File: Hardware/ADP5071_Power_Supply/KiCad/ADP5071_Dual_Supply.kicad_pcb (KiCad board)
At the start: 2 copper layers, 59.4 x 36.9 mm, 43 parts, among them J1 MountingPin, J2 Screw_Terminal_01x02, J3 Conn_01x03_Pin, J4 MountingPin, J5 MountingPin, J6 MountingPin, U1 ADP5071AREZ

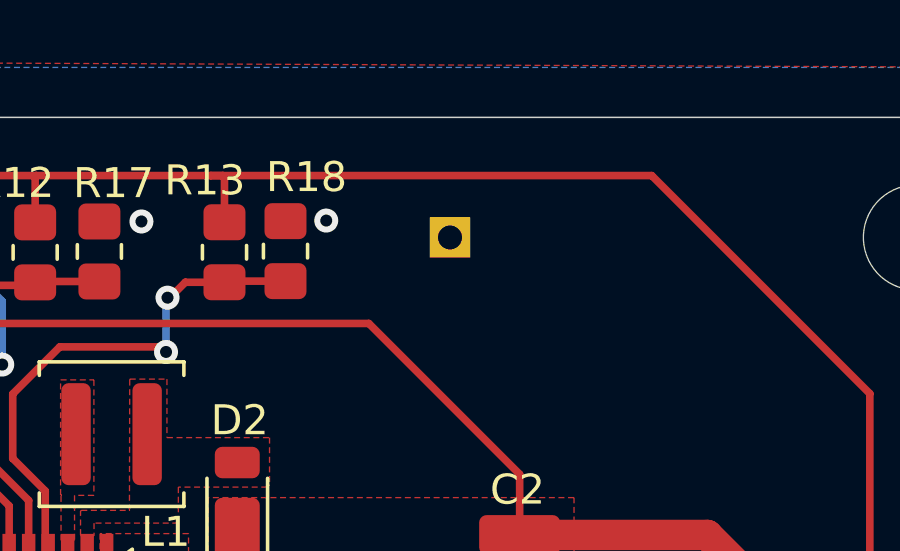
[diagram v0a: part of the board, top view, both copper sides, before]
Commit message: Fixed mounting asymmetry
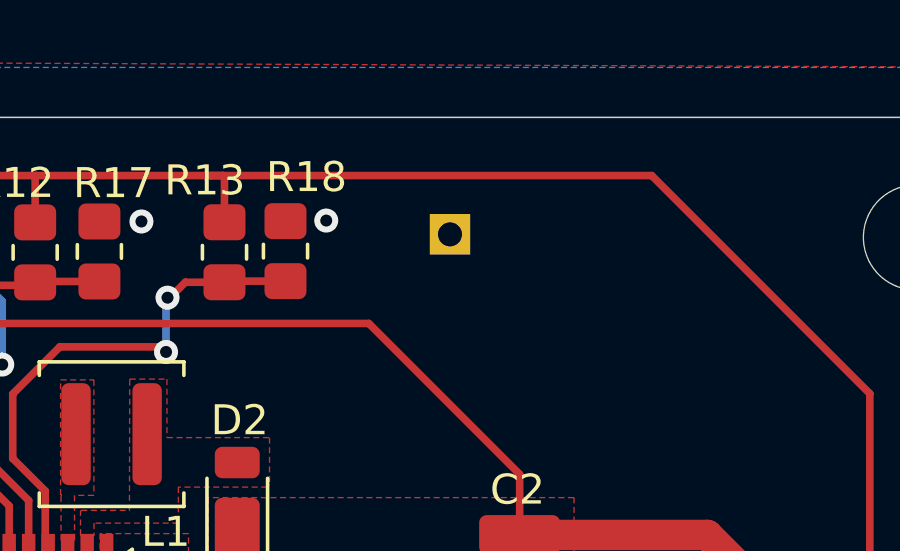
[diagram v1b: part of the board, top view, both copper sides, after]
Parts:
- moved J5 0.10 mm to (93.0, 69.0)
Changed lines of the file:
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@@
 	(footprint "Connector_PinSocket_2.00mm:PinSocket_1x01_P2.00mm_Vertical"
 		(layer "B.Cu")
-		(at 93 69.1034)
+		(at 93 69.0004)
 		(descr "Through hole straight socket strip, 1x01, 2.00mm pitch, single row (from Kicad 4.0.7), script generated")
 		(tags "Through hole socket strip THT 1x01 2.00mm single row")

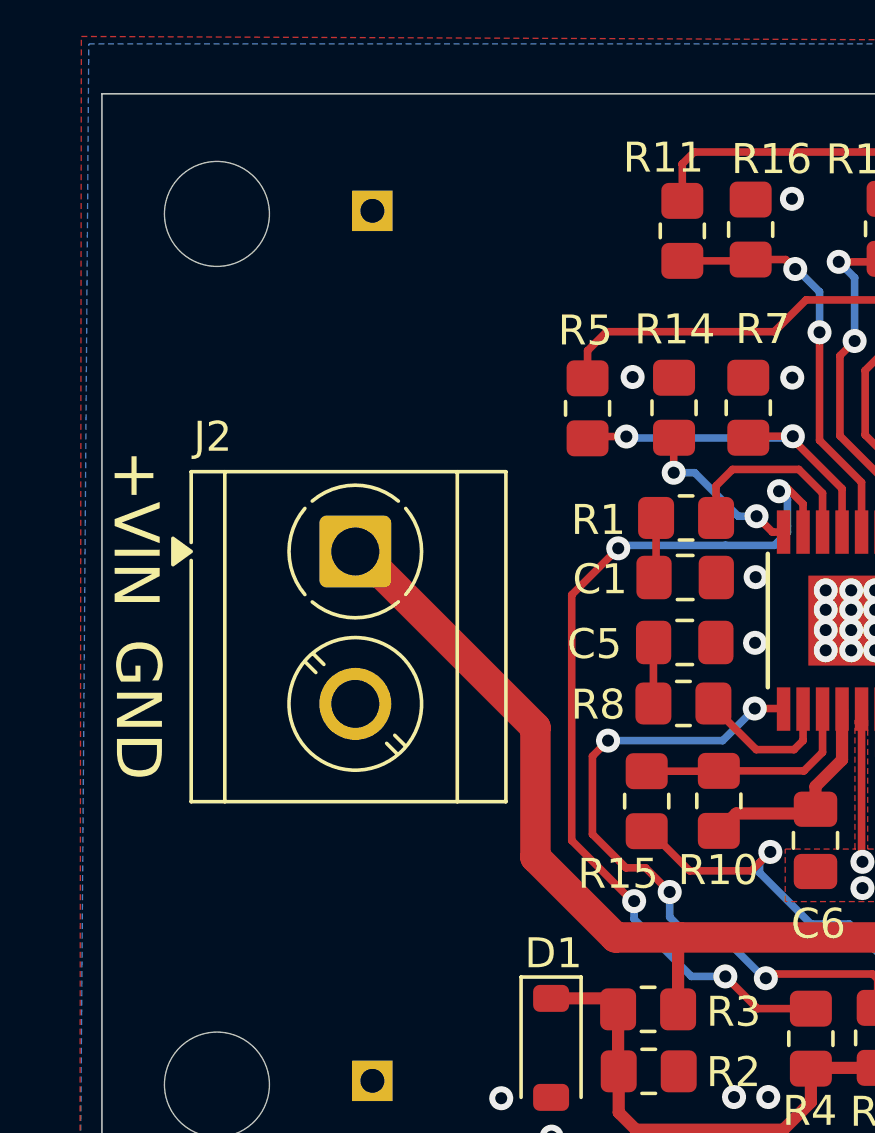
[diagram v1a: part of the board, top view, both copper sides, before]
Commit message: Waveguide + ground planes and P.S. daughter board modification
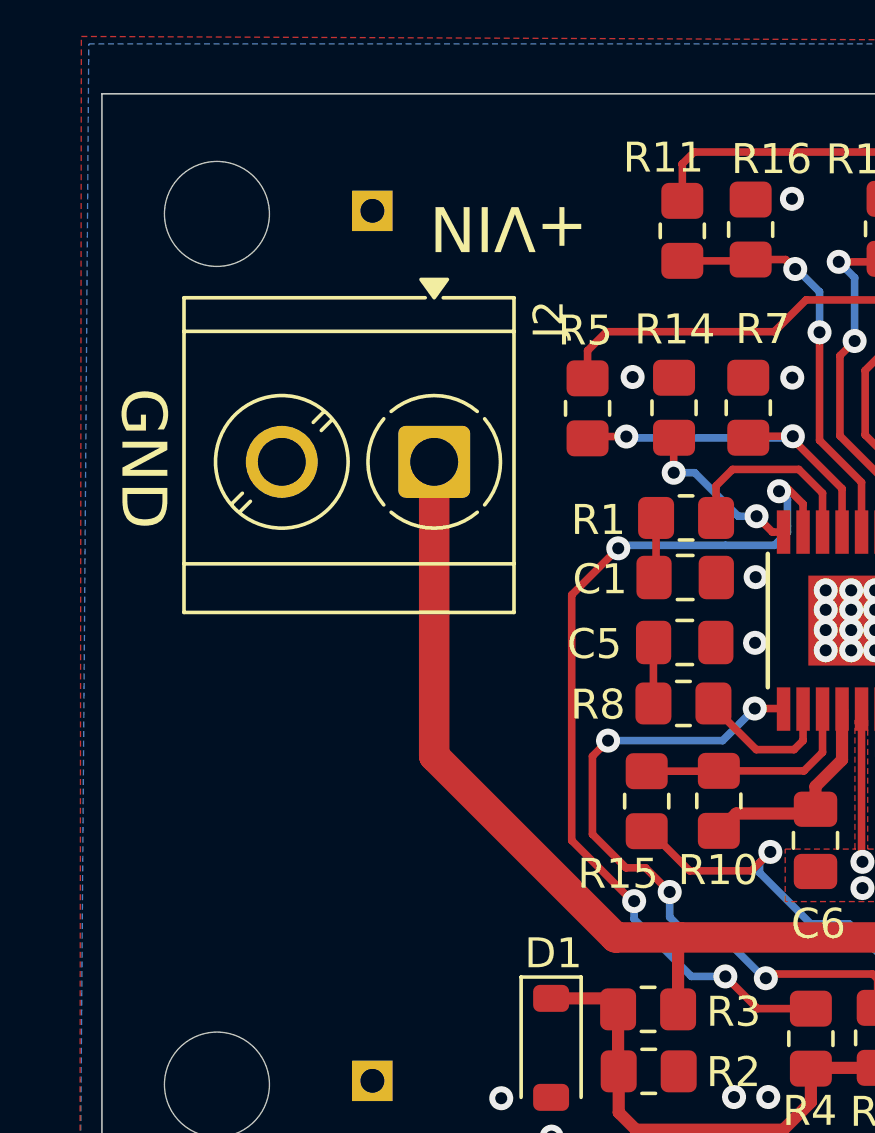
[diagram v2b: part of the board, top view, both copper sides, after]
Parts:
- moved J2 3.98 mm to (64.1, 77.4), turned to 180 degrees
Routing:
- net /VIN: track 49.9 -> 51.7 mm
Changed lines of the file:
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@@
 	(footprint "TerminalBlock_CUI:TerminalBlock_CUI_TB007-508-02_1x02_P5.08mm_Horizontal"
 		(layer "F.Cu")
-		(at 61.4296 80.3554 -90)
+		(at 64.060001 77.3675 180)
 		(descr "Terminal Block CUI TB007-508-02, 2 pins, pitch 5.08mm, size 10.8x10.2mm, drill diameter 1.6mm, pad diameter 2.4mm, https://www.cuidevices.com/product/resource/tb007-508.pdf, script-generated using https://gitlab.com/kicad/libraries/kicad-footprint-generator/scripts/TerminalBlock_CUI")
 		(tags "THT Terminal Block CUI TB007-508-02 pitch 5.08mm size 10.8x10.2mm drill 1.6mm pad 2.4mm")
 		(property "Reference" "J2"
-			(at -3.8206 4.7498 180)
+			(at -3.8206 4.7498 90)
 			(layer "F.SilkS")
 			(effects
@@
 		)
 		(property "Value" "Screw_Terminal_01x02"
-			(at 2.84 6.47 90)
+			(at 2.84 6.47 0)
 			(layer "F.Fab")
 			(effects
@@
 		)
 		(property "Datasheet" "~"
-			(at 0 0 90)
+			(at 0 0 0)
 			(layer "F.Fab")
 			(hide yes)
@@
 		)
 		(property "Description" "Generic screw terminal, single row, 01x02, script generated (kicad-library-utils/schlib/autogen/connector/)"
-			(at 0 0 90)
+			(at 0 0 0)
 			(layer "F.Fab")
 			(hide yes)
@@
 		(attr through_hole)
 		(fp_line
-			(start -2.66 5.47)
-			(end -0.3 5.47)
+			(start 8.340001 -5.02)
+			(end 8.34 5.470001)
 			(stroke
 				(width 0.12)
@@
 		)
 		(fp_line
-			(start 0.3 5.47)
-			(end 8.34 5.470001)
+			(start 6.756 -1.406001)
+			(end 6.394999 -1.045)
 			(stroke
 				(width 0.12)
@@
 		)
 		(fp_line
-			(start -2.660001 4.35)
-			(end 8.34 4.35)
+			(start 6.486001 -1.676)
+			(end 6.126001 -1.315)
 			(stroke
 				(width 0.12)
@@
 		)
 		(fp_line
-			(start 6.756 -1.406001)
-			(end 6.394999 -1.045)
+			(start 0.3 5.47)
+			(end 8.34 5.470001)
 			(stroke
 				(width 0.12)
@@
 		)
 		(fp_line
-			(start 6.486001 -1.676)
-			(end 6.126001 -1.315)
+			(start -2.66 5.47)
+			(end -0.3 5.47)
 			(stroke
 				(width 0.12)
@@
 		(fp_line
 			(start -2.66 -5.02)
-			(end -2.66 5.47)
+			(end 8.340001 -5.02)
 			(stroke
 				(width 0.12)
@@
 		(fp_line
 			(start -2.66 -5.02)
-			(end 8.340001 -5.02)
+			(end -2.66 5.47)
 			(stroke
 				(width 0.12)
@@
 		)
 		(fp_line
-			(start 8.340001 -5.02)
-			(end 8.34 5.470001)
+			(start -2.660001 4.35)
+			(end 8.34 4.35)
 			(stroke
 				(width 0.12)
@@
 		)
 		(fp_arc
-			(start 1.436 1.68)
-			(mid 0.000105 2.21009)
-			(end -1.43584 1.680136)
+			(start 1.68 -1.436)
+			(mid 2.21009 -0.000105)
+			(end 1.680136 1.43584)
 			(stroke
 				(width 0.12)
@@
 		)
 		(fp_arc
-			(start -1.68 1.436)
-			(mid -2.21009 0.000105)
-			(end -1.680136 -1.43584)
+			(start 1.436 1.68)
+			(mid 0.000105 2.21009)
+			(end -1.43584 1.680136)
 			(stroke
 				(width 0.12)
@@
 		)
 		(fp_arc
-			(start 1.68 -1.436)
-			(mid 2.21009 -0.000105)
-			(end 1.680136 1.43584)
+			(start -1.436 -1.68)
+			(mid -0.000105 -2.21009)
+			(end 1.43584 -1.680136)
 			(stroke
 				(width 0.12)
@@
 		)
 		(fp_arc
-			(start -1.436 -1.68)
-			(mid -0.000105 -2.21009)
-			(end 1.43584 -1.680136)
+			(start -1.68 1.436)
+			(mid -2.21009 0.000105)
+			(end -1.680136 -1.43584)
 			(stroke
 				(width 0.12)
@@
 		)
 		(fp_line
-			(start -3.04 5.85)
-			(end 8.72 5.85)
+			(start 8.720001 -5.4)
+			(end -3.04 -5.4)
 			(stroke
 				(width 0.05)
@@
 		)
 		(fp_line
-			(start -3.04 -5.4)
-			(end -3.04 5.85)
+			(start -3.04 5.85)
+			(end 8.72 5.85)
 			(stroke
 				(width 0.05)
@@
 		)
 		(fp_line
-			(start 8.720001 -5.4)
-			(end -3.04 -5.4)
+			(start -3.04 -5.4)
+			(end -3.04 5.85)
 			(stroke
 				(width 0.05)
@@
 		)
 		(fp_line
-			(start -1.54 5.35)
-			(end -2.54 4.35)
+			(start 8.22 5.35)
+			(end -1.54 5.35)
 			(stroke
 				(width 0.1)
@@
 		)
 		(fp_line
-			(start 8.22 5.35)
-			(end -1.54 5.35)
+			(start 8.22 -4.9)
+			(end 8.22 5.35)
 			(stroke
 				(width 0.1)
@@
 		)
 		(fp_line
-			(start -2.54 4.35)
-			(end 8.22 4.35)
+			(start 6.483 -1.177)
+			(end 3.903 1.403)
 			(stroke
 				(width 0.1)
@@
 		)
 		(fp_line
-			(start -2.54 4.35)
-			(end -2.54 -4.9)
+			(start 6.257 -1.403)
+			(end 3.677 1.177)
 			(stroke
 				(width 0.1)
@@
 		)
 		(fp_line
-			(start 6.483 -1.177)
-			(end 3.903 1.403)
+			(start 1.177 -1.403)
+			(end -1.403 1.177)
 			(stroke
 				(width 0.1)
@@
 		)
 		(fp_line
-			(start 1.177 -1.403)
-			(end -1.403 1.177)
+			(start -1.54 5.35)
+			(end -2.54 4.35)
 			(stroke
 				(width 0.1)
@@
 		)
 		(fp_line
-			(start 6.257 -1.403)
-			(end 3.677 1.177)
+			(start -2.54 4.35)
+			(end 8.22 4.35)
 			(stroke
 				(width 0.1)
@@
 		)
 		(fp_line
-			(start -2.54 -3.4)
-			(end 8.22 -3.4)
+			(start -2.54 4.35)
+			(end -2.54 -4.9)
 			(stroke
 				(width 0.1)
@@
 		)
 		(fp_line
-			(start -2.54 -4.9)
-			(end 8.22 -4.9)
+			(start -2.54 -3.4)
+			(end 8.22 -3.4)
 			(stroke
 				(width 0.1)
@@
 		)
 		(fp_line
-			(start 8.22 -4.9)
-			(end 8.22 5.35)
+			(start -2.54 -4.9)
+			(end 8.22 -4.9)
 			(stroke
 				(width 0.1)
@@
 		)
 		(fp_circle
-			(center 0 0)
-			(end 1.850001 0)
+			(center 5.079999 0)
+			(end 6.93 0)
 			(stroke
 				(width 0.1)
@@
 		)
 		(fp_circle
-			(center 5.079999 0)
-			(end 6.93 0)
+			(center 0 0)
+			(end 1.850001 0)
 			(stroke
 				(width 0.1)
@@
 		)
 		(fp_text user "${REFERENCE}"
-			(at 2.84 0.225 90)
+			(at 2.84 0.225 0)
 			(layer "F.Fab")
 			(effects
@@
 		)
 		(pad "1" thru_hole roundrect
-			(at 0 0 270)
+			(at 0 0 180)
 			(size 2.4 2.4)
 			(drill 1.6)
@@
 		)
 		(pad "2" thru_hole circle
-			(at 5.079999 0 270)
+			(at 5.079999 0 180)
 			(size 2.4 2.4)
 			(drill 1.6)
@@
 	)
 	(gr_text "+VIN"
-		(at 54.103 79.602 270)
+		(at 66.54 69.57 180)
 		(layer "F.SilkS")
 		(effects
@@
 	)
 	(gr_text "GND"
-		(at 54.178 85.627 270)
+		(at 54.36 77.26 270)
 		(layer "F.SilkS")
 		(effects
@@
 	)
 	(segment
+		(start 64.060001 87.175601)
+		(end 64.060001 77.3675)
+		(width 1.016)
+		(layer "F.Cu")
+		(net 4)
+	)
+	(segment
 		(start 80.3944 94.1)
 		(end 80.3944 93.22)
@@
 	)
 	(segment
-		(start 67.4344 90.55)
-		(end 70.1044 93.22)
-		(width 1.016)
-		(layer "F.Cu")
-		(net 4)
-	)
-	(segment
 		(start 80.148897 87.355503)
 		(end 80.442094 87.6487)
@@
 	)
 	(segment
-		(start 67.4344 86.22)
-		(end 67.4344 90.55)
-		(width 1.016)
-		(layer "F.Cu")
-		(net 4)
-	)
-	(segment
 		(start 79.605 85.6084)
 		(end 79.605 86.811606)
@@
 	)
 	(segment
+		(start 72.2444 93.22)
+		(end 70.1044 93.22)
+		(width 1.016)
+		(layer "F.Cu")
+		(net 4)
+	)
+	(segment
 		(start 80.905 87.5393)
 		(end 81.0144 87.6487)
@@
 	)
 	(segment
+		(start 70.1044 93.22)
+		(end 64.060001 87.175601)
+		(width 1.016)
+		(layer "F.Cu")
+		(net 4)
+	)
+	(segment
 		(start 80.905 85.6084)
 		(end 80.905 87.5393)
@@
 	)
 	(segment
-		(start 61.5698 80.3554)
-		(end 67.4344 86.22)
-		(width 1.016)
-		(layer "F.Cu")
-		(net 4)
-	)
-	(segment
 		(start 80.3944 93.22)
 		(end 80.8444 93.22)
@@
 	)
 	(segment
-		(start 70.1044 93.22)
-		(end 72.2444 93.22)
-		(width 1.016)
-		(layer "F.Cu")
-		(net 4)
-	)
-	(segment
 		(start 80.671602 94.377202)
 		(end 80.3944 94.1)
@@
 		(layer "F.Cu")
 		(net 4)
-	)
-	(segment
-		(start 61.4296 80.3554)
-		(end 61.5698 80.3554)
-		(width 1.016)
-		(layer "F.Cu")
-		(net 4)

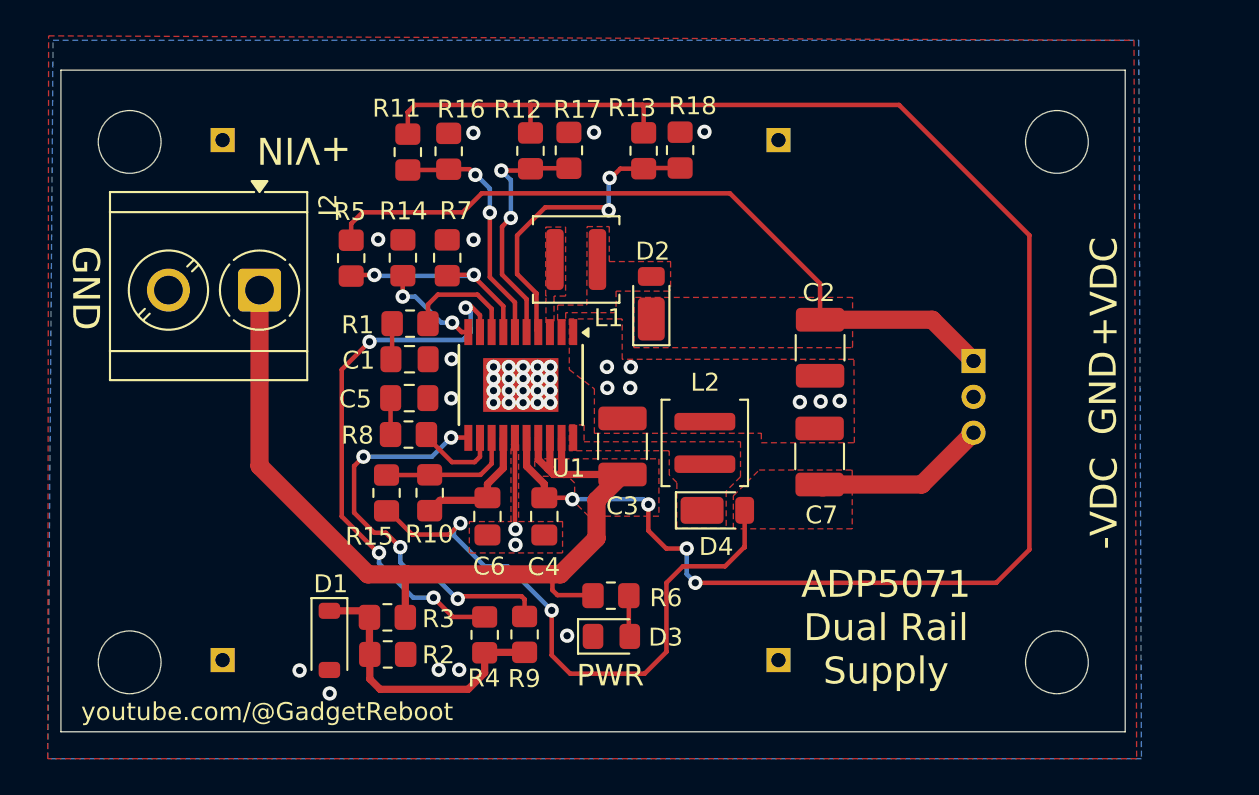
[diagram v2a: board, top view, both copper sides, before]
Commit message: Ease of construction, added new layers, prelimininary routing.
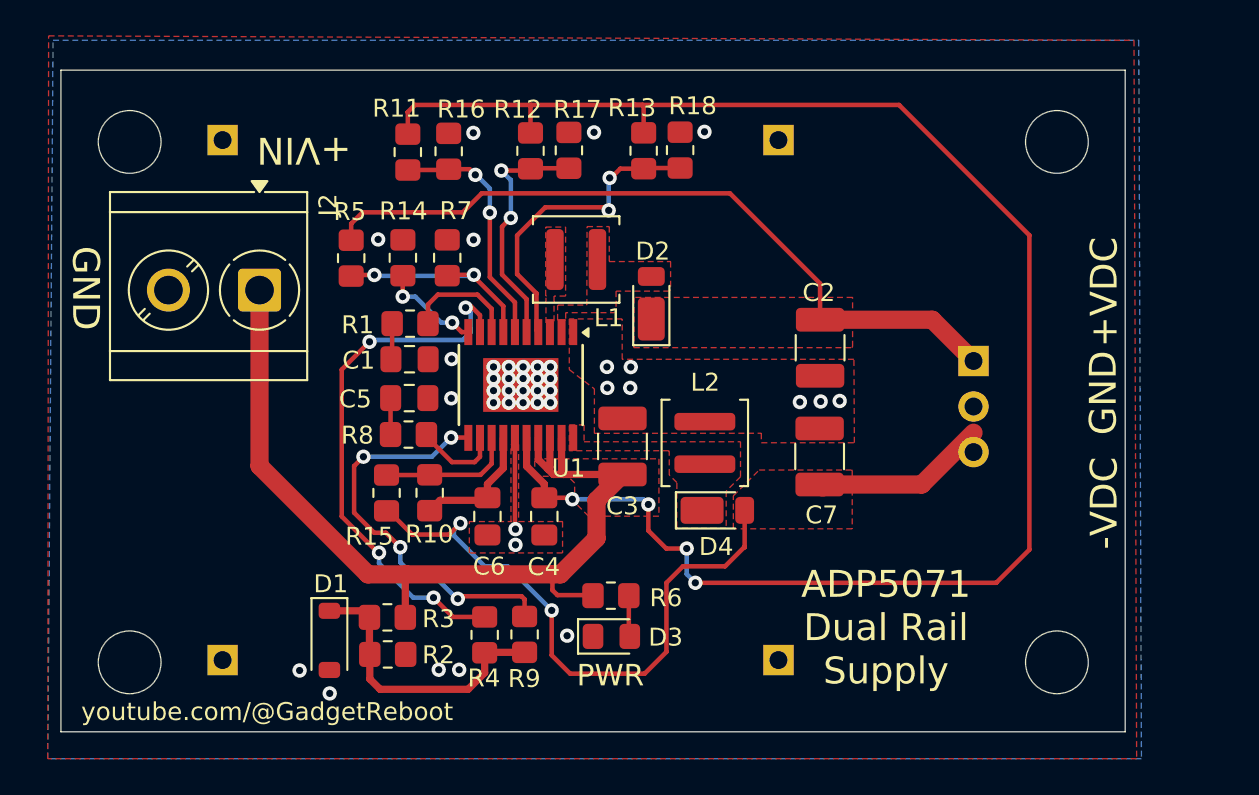
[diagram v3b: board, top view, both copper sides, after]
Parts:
- J1, J4, J5, J6: footprint Connector_PinSocket_2.00mm:PinSocket_1x01_P2.00mm_Vertical -> Connector_PinSocket_2.54mm:PinSocket_1x01_P2.54mm_Vertical
- J3: footprint Connector_PinHeader_2.00mm:PinHeader_1x03_P2.00mm_Vertical -> Connector_PinHeader_2.54mm:PinHeader_1x03_P2.54mm_Vertical

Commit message: added connector for dual board power delivery
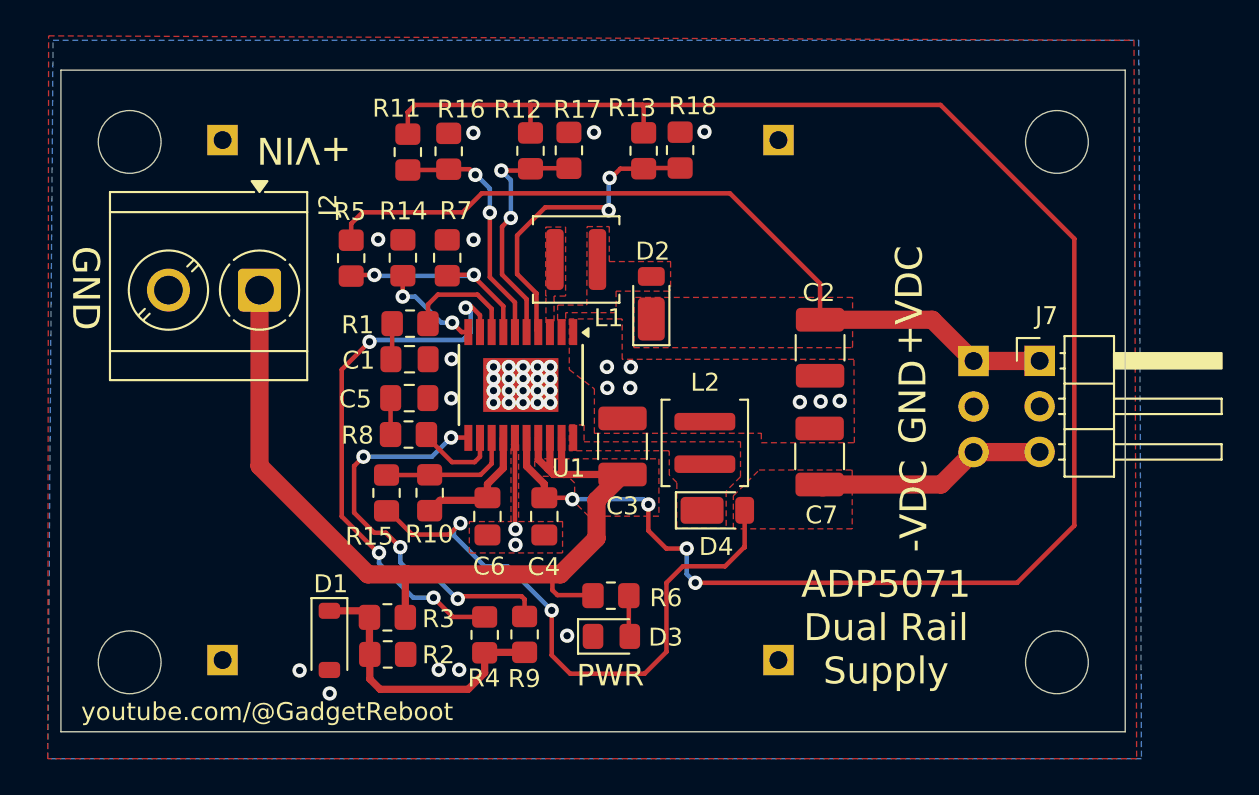
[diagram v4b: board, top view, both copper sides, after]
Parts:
- added J7: Conn_01x03_Pin, Connector_PinHeader_2.54mm:PinHeader_1x03_P2.54mm_Horizontal, F.Cu at (107.6, 81.3)
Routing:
- net Net-(U1-VREG): track 95.4 -> 99.5 mm
- net +VDC: track 41.4 -> 45.1 mm, vias 0 -> 21
- net -VDC: track 43.9 -> 47.2 mm
- net GNDREF: vias 41 -> 20
- removed copper zone on F.Cu, net -VDC
